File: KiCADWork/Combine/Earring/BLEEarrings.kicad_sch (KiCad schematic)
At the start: 5 parts, among them J3 USB_C_Receptacle, SW1 TK-6580B-1

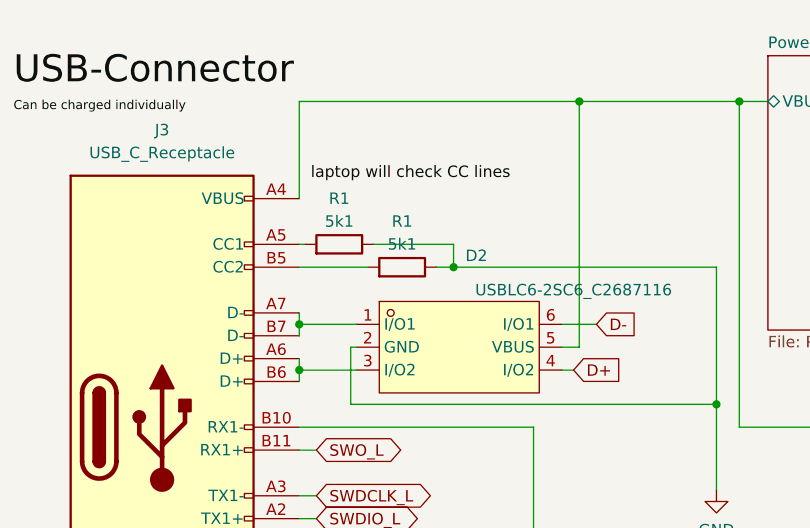
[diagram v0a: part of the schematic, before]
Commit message: Completing the combined layout
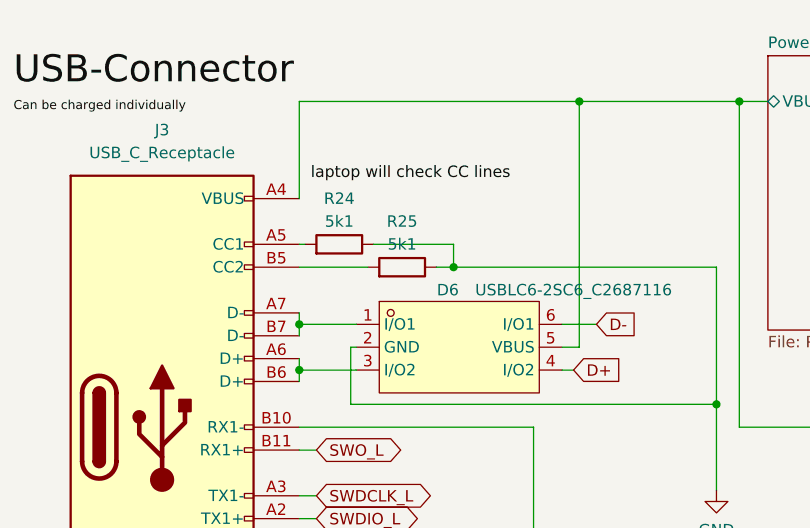
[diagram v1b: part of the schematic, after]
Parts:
- renumbered D2 to D6, R1 to R24, R1 to R25
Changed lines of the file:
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@@
   (symbol (lib_id "easyeda2kicad:USBLC6-2SC6_C2687116") (at 109.855 85.725 0) (unit 1)
     (in_bom yes) (on_board yes) (dnp no)
-    (property "Reference" "D2" (at 111.76 75.565 0)
+    (property "Reference" "D6" (at 108.585 79.375 0)
       (effects (font (size 1.27 1.27)))
     )
@@
       (project "Combine"
         (path "/3a067f6e-27d8-46f5-91e9-67d8f6f5da54/8babb549-cb41-41ef-aae8-a9df69f93513"
-          (reference "D2") (unit 1)
-        )
-        (path "/3a067f6e-27d8-46f5-91e9-67d8f6f5da54/e248df4f-814c-46e0-8ef1-d7e76ca8fad7"
-          (reference "D3") (unit 1)
+          (reference "D6") (unit 1)
+        )
+        (path "/3a067f6e-27d8-46f5-91e9-67d8f6f5da54/e248df4f-814c-46e0-8ef1-d7e76ca8fad7"
+          (reference "D9") (unit 1)
         )
       )
@@
   (symbol (lib_id "Device:R") (at 96.52 74.295 270) (mirror x) (unit 1)
     (in_bom yes) (on_board yes) (dnp no)
-    (property "Reference" "R1" (at 96.52 69.215 90)
+    (property "Reference" "R24" (at 96.52 69.215 90)
       (effects (font (size 1.27 1.27)))
     )
@@
       (project "Combine"
         (path "/3a067f6e-27d8-46f5-91e9-67d8f6f5da54/8babb549-cb41-41ef-aae8-a9df69f93513"
-          (reference "R1") (unit 1)
-        )
-        (path "/3a067f6e-27d8-46f5-91e9-67d8f6f5da54/e248df4f-814c-46e0-8ef1-d7e76ca8fad7"
-          (reference "R10") (unit 1)
+          (reference "R24") (unit 1)
+        )
+        (path "/3a067f6e-27d8-46f5-91e9-67d8f6f5da54/e248df4f-814c-46e0-8ef1-d7e76ca8fad7"
+          (reference "R38") (unit 1)
         )
       )
@@
   (symbol (lib_id "power:+BATT") (at 243.84 66.04 0) (unit 1)
     (in_bom yes) (on_board yes) (dnp no) (fields_autoplaced)
-    (property "Reference" "#PWR02" (at 243.84 69.85 0)
+    (property "Reference" "#PWR032" (at 243.84 69.85 0)
       (effects (font (size 1.27 1.27)) hide)
     )
@@
       (project "Combine"
         (path "/3a067f6e-27d8-46f5-91e9-67d8f6f5da54/8babb549-cb41-41ef-aae8-a9df69f93513"
-          (reference "#PWR02") (unit 1)
-        )
-        (path "/3a067f6e-27d8-46f5-91e9-67d8f6f5da54/e248df4f-814c-46e0-8ef1-d7e76ca8fad7"
           (reference "#PWR032") (unit 1)
+        )
+        (path "/3a067f6e-27d8-46f5-91e9-67d8f6f5da54/e248df4f-814c-46e0-8ef1-d7e76ca8fad7"
+          (reference "#PWR059") (unit 1)
         )
       )
@@
   (symbol (lib_id "Device:R") (at 103.505 76.835 270) (mirror x) (unit 1)
     (in_bom yes) (on_board yes) (dnp no)
-    (property "Reference" "R1" (at 103.505 71.755 90)
+    (property "Reference" "R25" (at 103.505 71.755 90)
       (effects (font (size 1.27 1.27)))
     )
@@
       (project "Combine"
         (path "/3a067f6e-27d8-46f5-91e9-67d8f6f5da54/8babb549-cb41-41ef-aae8-a9df69f93513"
-          (reference "R1") (unit 1)
-        )
-        (path "/3a067f6e-27d8-46f5-91e9-67d8f6f5da54/e248df4f-814c-46e0-8ef1-d7e76ca8fad7"
-          (reference "R11") (unit 1)
+          (reference "R25") (unit 1)
+        )
+        (path "/3a067f6e-27d8-46f5-91e9-67d8f6f5da54/e248df4f-814c-46e0-8ef1-d7e76ca8fad7"
+          (reference "R39") (unit 1)
         )
       )
@@
         )
         (path "/3a067f6e-27d8-46f5-91e9-67d8f6f5da54/e248df4f-814c-46e0-8ef1-d7e76ca8fad7"
-          (reference "J4") (unit 1)
+          (reference "J6") (unit 1)
         )
       )
@@
   (symbol (lib_id "power:GND") (at 138.43 101.6 0) (unit 1)
     (in_bom yes) (on_board yes) (dnp no) (fields_autoplaced)
-    (property "Reference" "#PWR023" (at 138.43 107.95 0)
+    (property "Reference" "#PWR031" (at 138.43 107.95 0)
       (effects (font (size 1.27 1.27)) hide)
     )
@@
       (project "Combine"
         (path "/3a067f6e-27d8-46f5-91e9-67d8f6f5da54/8babb549-cb41-41ef-aae8-a9df69f93513"
+          (reference "#PWR031") (unit 1)
+        )
+        (path "/3a067f6e-27d8-46f5-91e9-67d8f6f5da54/e248df4f-814c-46e0-8ef1-d7e76ca8fad7"
+          (reference "#PWR058") (unit 1)
+        )
+      )
+      (project "BLEEarrings"
+        (path "/fde3e4b3-cb63-4f5f-903c-f7733537b674"
           (reference "#PWR023") (unit 1)
         )
-        (path "/3a067f6e-27d8-46f5-91e9-67d8f6f5da54/e248df4f-814c-46e0-8ef1-d7e76ca8fad7"
-          (reference "#PWR031") (unit 1)
-        )
-      )
-      (project "BLEEarrings"
-        (path "/fde3e4b3-cb63-4f5f-903c-f7733537b674"
-          (reference "#PWR023") (unit 1)
-        )
       )
     )
@@
   (symbol (lib_id "power:GND") (at 73.025 138.43 0) (unit 1)
     (in_bom yes) (on_board yes) (dnp no) (fields_autoplaced)
-    (property "Reference" "#PWR01" (at 73.025 144.78 0)
+    (property "Reference" "#PWR030" (at 73.025 144.78 0)
       (effects (font (size 1.27 1.27)) hide)
     )
@@
       (project "Combine"
         (path "/3a067f6e-27d8-46f5-91e9-67d8f6f5da54/8babb549-cb41-41ef-aae8-a9df69f93513"
-          (reference "#PWR01") (unit 1)
-        )
-        (path "/3a067f6e-27d8-46f5-91e9-67d8f6f5da54/e248df4f-814c-46e0-8ef1-d7e76ca8fad7"
           (reference "#PWR030") (unit 1)
         )
-      )
+        (path "/3a067f6e-27d8-46f5-91e9-67d8f6f5da54/e248df4f-814c-46e0-8ef1-d7e76ca8fad7"
+          (reference "#PWR057") (unit 1)
+        )
+      )
